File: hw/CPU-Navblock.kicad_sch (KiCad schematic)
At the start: 32 parts, among them J4001 Conn_01x08, J4002 Conn_01x03, J4003 Conn_01x02, J4004 Conn_01x02, J4005 Conn_01x02, J4006 Conn_01x02, U4000 STM32F401XX-LQFP64, U4001 TLV62150A, Y4000 MCSJK-7I-8.00-18-30-60-B-30

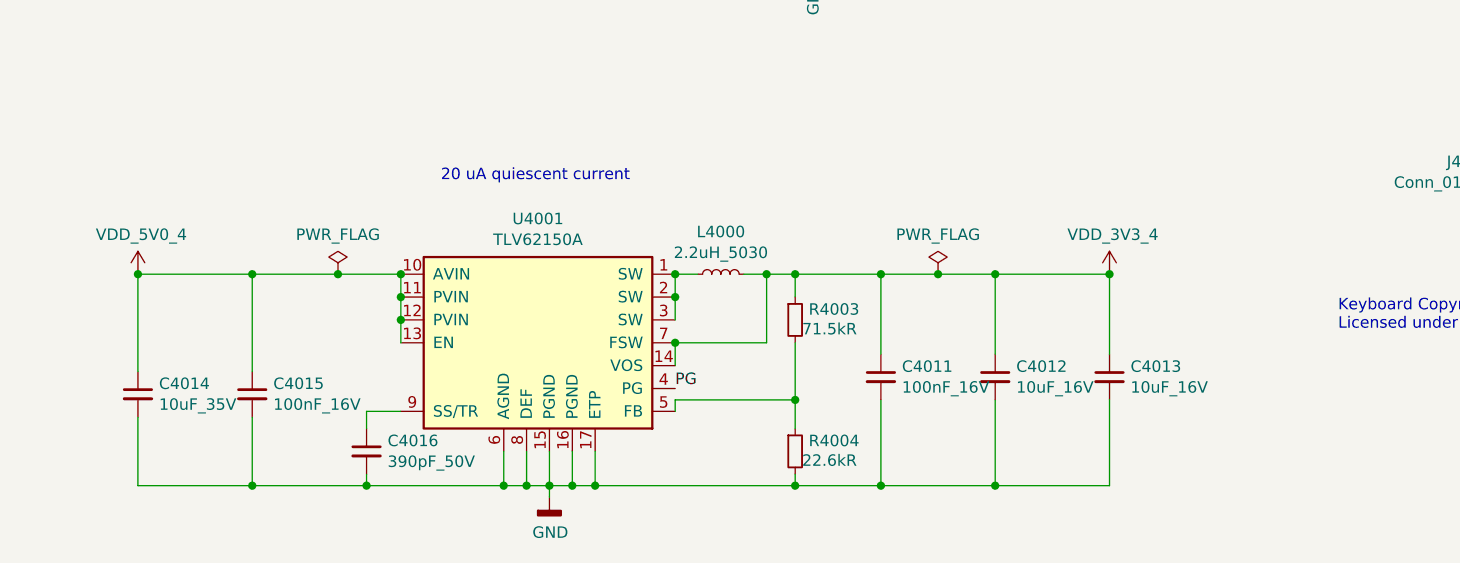
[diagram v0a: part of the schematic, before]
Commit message: Add current probes to 3.3V and pull-up to LV_EN.
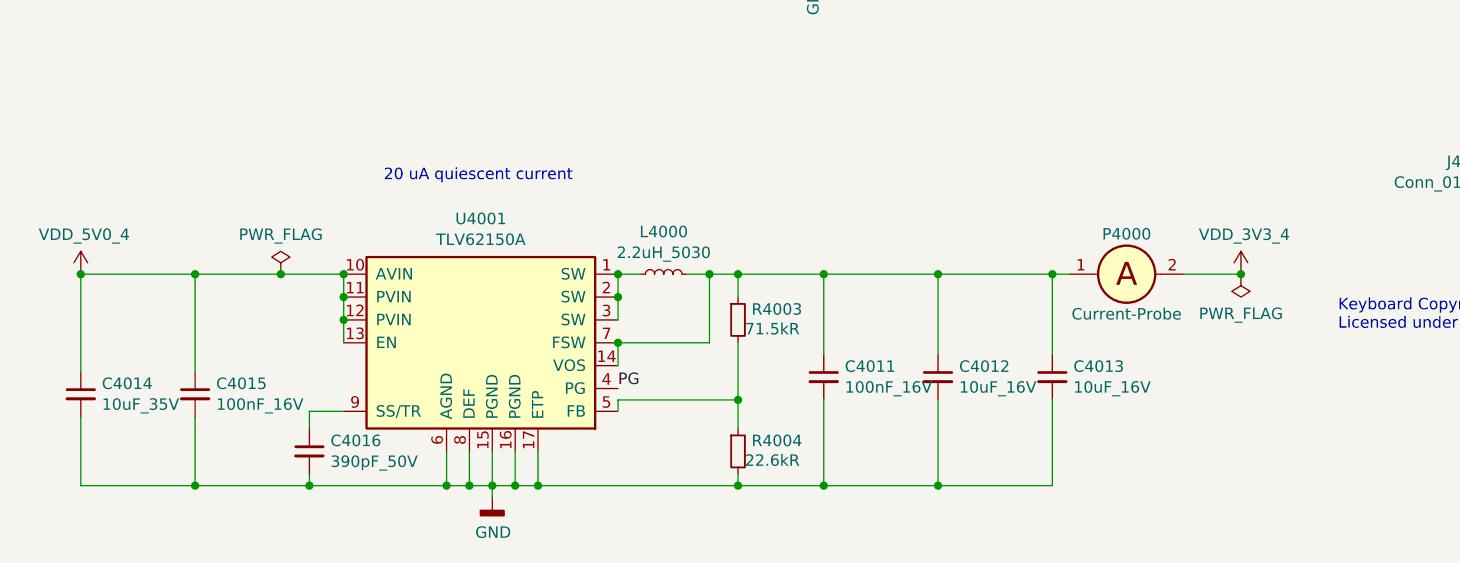
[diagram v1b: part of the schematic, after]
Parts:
- added P4000: Current-Probe, Keyboard:Current-Probe-2.54, symbol Keyboard:Current-Probe
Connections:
- net VDD_3V3_4: now also P4000.2; no longer C4011.1, C4012.1, C4013.1, L4000.2, R4003.1, U4001.14 (VOS), U4001.7 (FSW)
- new net: C4011.1, C4012.1, C4013.1, L4000.2, P4000.1, R4003.1, U4001.14 (VOS), U4001.7 (FSW)
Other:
- moved on the sheet: C4011, C4012, C4013, C4014, C4015, C4016, L4000, R4003, R4004, U4001
